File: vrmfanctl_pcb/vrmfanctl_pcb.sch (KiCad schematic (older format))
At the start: 7 parts, among them J1 SATA Power Male, J2 Hole, J3 Pin socket L-shape, J4 Pin socket L-shape, U1 ATtiny85-20PU

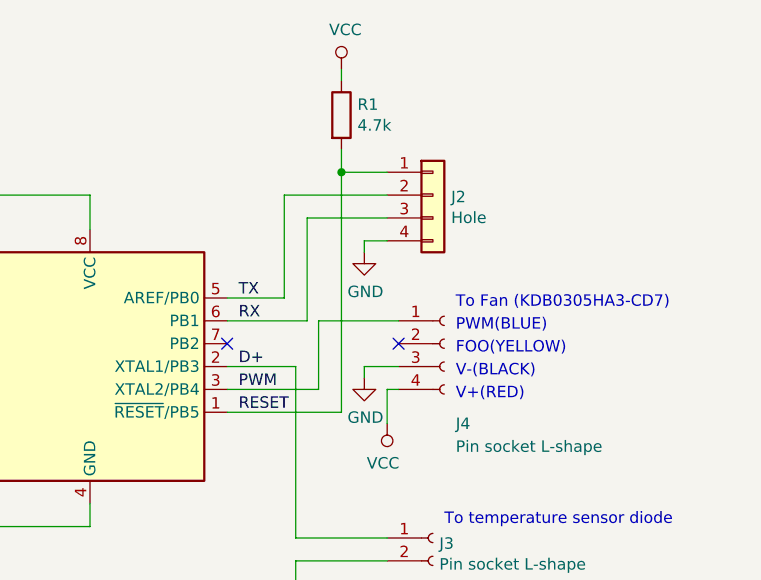
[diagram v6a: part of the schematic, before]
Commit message: rewrite firmware and update pcb
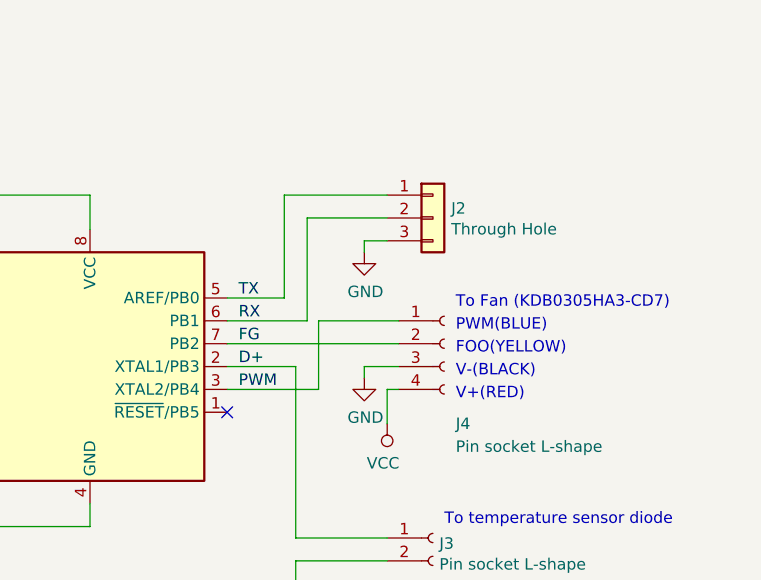
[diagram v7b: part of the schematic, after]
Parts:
- removed J2: Hole, Connector_PinHeader_2.54mm:PinHeader_1x04_P2.54mm_Vertical, symbol Connector_Generic:Conn_01x04
- removed R1: 4.7k, Resistor_THT:R_Axial_DIN0204_L3.6mm_D1.6mm_P5.08mm_Horizontal, symbol Device:R
- added J2: Through Hole, Connector_PinHeader_2.54mm:PinHeader_1x03_P2.54mm_Vertical, symbol Connector_Generic:Conn_01x03
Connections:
- net GND: now also J2.3 (Pin_3)
- net RX: now also J2.2 (Pin_2)
- net TX: now also J2.1 (Pin_1)
- net FG: now reaches U1.7 (PB2)
- net FG: now also J4.2 (Pin_2)
- net RESET: no longer names the net of U1.1 (~RESET~/PB5)
- no-connect marks 11 -> 10
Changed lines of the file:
@@
 EESchema Schematic File Version 4
 LIBS:vrmfanctl_pcb-cache
-EELAYER 26 0
+EELAYER 30 0
 EELAYER END
 $Descr A4 11693 8268
@@
 $EndComp
 $Comp
+L power:GND #PWR06
+U 1 1 5D600CEB
+P 5700 1600
+F 0 "#PWR06" H 5700 1350 50  0001 C CNN
+F 1 "GND" H 5705 1427 50  0000 C CNN
+F 2 "" H 5700 1600 50  0001 C CNN
+F 3 "" H 5700 1600 50  0001 C CNN
+	1    5700 1600
+	1    0    0    -1
+$EndComp
+Wire Wire Line
+	5800 1550 5700 1550
+Wire Wire Line
+	5700 1550 5700 1600
+Wire Wire Line
+	5350 1350 5350 1800
+Wire Wire Line
+	5350 1800 5100 1800
+Wire Wire Line
+	5350 1350 5800 1350
+Text Label 5150 1800 0    50   ~ 0
+TX
+Text Label 5150 1900 0    50   ~ 0
+RX
+Wire Wire Line
+	5100 1900 5450 1900
+Wire Wire Line
+	5450 1900 5450 1450
+Wire Wire Line
+	5450 1450 5800 1450
+Wire Wire Line
+	5850 1900 5500 1900
+Text Notes 6050 2800 0    50   ~ 0
+To temperature sensor diode
+Text Label 5150 2100 0    50   ~ 0
+D+
+Wire Wire Line
+	5400 2850 5800 2850
+Wire Wire Line
+	5400 2950 5400 3050
+Wire Wire Line
+	5800 2950 5400 2950
+$Comp
+L power:GND #PWR05
+U 1 1 5D614B08
+P 5400 3050
+F 0 "#PWR05" H 5400 2800 50  0001 C CNN
+F 1 "GND" H 5405 2877 50  0000 C CNN
+F 2 "" H 5400 3050 50  0001 C CNN
+F 3 "" H 5400 3050 50  0001 C CNN
+	1    5400 3050
+	1    0    0    -1
+$EndComp
+$Comp
+L Connector:Conn_01x02_Female J3
+U 1 1 5D610DF4
+P 6000 2850
+F 0 "J3" H 6028 2826 50  0000 L CNN
+F 1 "Pin socket L-shape" H 6028 2735 50  0000 L CNN
+F 2 "Connector_PinSocket_2.54mm:PinSocket_1x02_P2.54mm_Horizontal" H 6000 2850 50  0001 C CNN
+F 3 "~" H 6000 2850 50  0001 C CNN
+	1    6000 2850
+	1    0    0    -1
+$EndComp
+Wire Wire Line
+	5500 2200 5400 2200
+Wire Wire Line
+	5400 2200 5100 2200
+Wire Wire Line
+	5400 2100 5100 2100
+Wire Wire Line
+	5400 2100 5400 2850
+Wire Wire Line
+	5500 1900 5500 2200
+$Comp
 L Connector:Conn_01x04_Female J4
 U 1 1 5D5F6860
@@
 	1    0    0    -1
 $EndComp
-$Comp
-L power:GND #PWR06
-U 1 1 5D600CEB
-P 5700 1600
-F 0 "#PWR06" H 5700 1350 50  0001 C CNN
-F 1 "GND" H 5705 1427 50  0000 C CNN
-F 2 "" H 5700 1600 50  0001 C CNN
-F 3 "" H 5700 1600 50  0001 C CNN
-	1    5700 1600
-	1    0    0    -1
-$EndComp
-Wire Wire Line
-	5800 1550 5700 1550
-Wire Wire Line
-	5700 1550 5700 1600
-Wire Wire Line
-	5350 1350 5350 1800
-Wire Wire Line
-	5350 1800 5100 1800
-Wire Wire Line
-	5350 1350 5800 1350
-Text Label 5150 1800 0    50   ~ 0
-TX
-Text Label 5150 1900 0    50   ~ 0
-RX
-Wire Wire Line
-	5100 1900 5450 1900
-Wire Wire Line
-	5450 1900 5450 1450
-Wire Wire Line
-	5450 1450 5800 1450
-Wire Wire Line
-	5850 1900 5500 1900
-Text Notes 6050 2800 0    50   ~ 0
-To temperature sensor diode
-Text Label 5150 2100 0    50   ~ 0
-D+
-Wire Wire Line
-	5400 2850 5800 2850
-Wire Wire Line
-	5400 2950 5400 3050
-Wire Wire Line
-	5800 2950 5400 2950
-$Comp
-L power:GND #PWR05
-U 1 1 5D614B08
-P 5400 3050
-F 0 "#PWR05" H 5400 2800 50  0001 C CNN
-F 1 "GND" H 5405 2877 50  0000 C CNN
-F 2 "" H 5400 3050 50  0001 C CNN
-F 3 "" H 5400 3050 50  0001 C CNN
-	1    5400 3050
-	1    0    0    -1
-$EndComp
-$Comp
-L Connector:Conn_01x02_Female J3
-U 1 1 5D610DF4
-P 6000 2850
-F 0 "J3" H 6028 2826 50  0000 L CNN
-F 1 "Pin socket L-shape" H 6028 2735 50  0000 L CNN
-F 2 "Connector_PinSocket_2.54mm:PinSocket_1x02_P2.54mm_Horizontal" H 6000 2850 50  0001 C CNN
-F 3 "~" H 6000 2850 50  0001 C CNN
-	1    6000 2850
-	1    0    0    -1
-$EndComp
-Wire Wire Line
-	5500 2200 5400 2200
-Wire Wire Line
-	5400 2200 5100 2200
-Wire Wire Line
-	5400 2100 5100 2100
-Wire Wire Line
-	5400 2100 5400 2850
-NoConn ~ 5100 2000
-NoConn ~ 5850 2000
-$Comp
-L Device:R R1
-U 1 1 5D62348B
-P 5600 1000
-F 0 "R1" H 5670 1046 50  0000 L CNN
-F 1 "4.7k" H 5670 955 50  0000 L CNN
-F 2 "Resistor_THT:R_Axial_DIN0204_L3.6mm_D1.6mm_P5.08mm_Horizontal" V 5530 1000 50  0001 C CNN
-F 3 "~" H 5600 1000 50  0001 C CNN
-	1    5600 1000
-	1    0    0    -1
-$EndComp
-$Comp
-L Connector_Generic:Conn_01x04 J2
-U 1 1 5D6235F9
-P 6000 1350
-F 0 "J2" H 6080 1342 50  0000 L CNN
-F 1 "Hole" H 6080 1251 50  0000 L CNN
-F 2 "Connector_PinHeader_2.54mm:PinHeader_1x04_P2.54mm_Vertical" H 6000 1350 50  0001 C CNN
-F 3 "~" H 6000 1350 50  0001 C CNN
-	1    6000 1350
-	1    0    0    -1
-$EndComp
-$Comp
-L power:VCC #PWR0103
-U 1 1 5D623D93
-P 5600 800
-F 0 "#PWR0103" H 5600 650 50  0001 C CNN
-F 1 "VCC" H 5617 973 50  0000 C CNN
-F 2 "" H 5600 800 50  0001 C CNN
-F 3 "" H 5600 800 50  0001 C CNN
-	1    5600 800
-	1    0    0    -1
-$EndComp
-Wire Wire Line
-	5600 800  5600 850
-Wire Wire Line
-	5600 1150 5600 1250
-Wire Wire Line
-	5600 1250 5800 1250
-Wire Wire Line
-	5500 1900 5500 2200
-Wire Wire Line
-	5600 1250 5600 2300
-Wire Wire Line
-	5600 2300 5100 2300
-Connection ~ 5600 1250
-Text Label 5150 2300 0    50   ~ 0
-RESET
+Wire Wire Line
+	5100 2000 5850 2000
+Text Label 5150 2000 0    50   ~ 0
+FG
+$Comp
+L Connector_Generic:Conn_01x03 J2
+U 1 1 5D6F20BE
+P 6000 1450
+F 0 "J2" H 6080 1492 50  0000 L CNN
+F 1 "Through Hole" H 6080 1401 50  0000 L CNN
+F 2 "Connector_PinHeader_2.54mm:PinHeader_1x03_P2.54mm_Vertical" H 6000 1450 50  0001 C CNN
+F 3 "~" H 6000 1450 50  0001 C CNN
+	1    6000 1450
+	1    0    0    -1
+$EndComp
+NoConn ~ 5100 2300
 $EndSCHEMATC

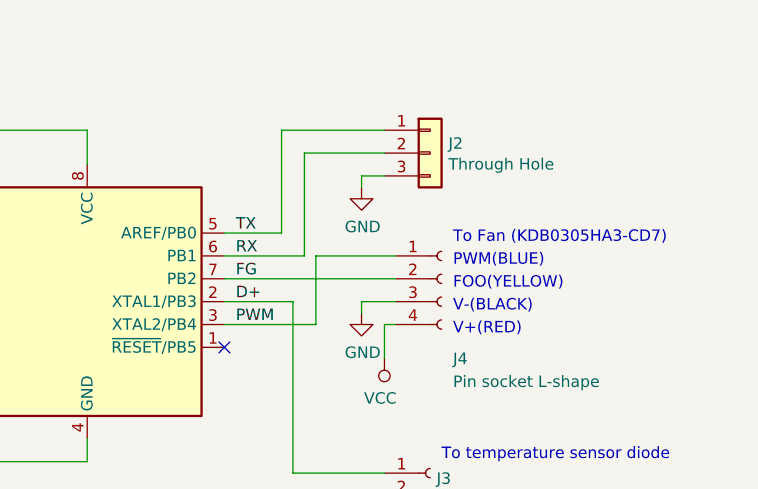
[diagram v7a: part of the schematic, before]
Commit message: change pcb layout
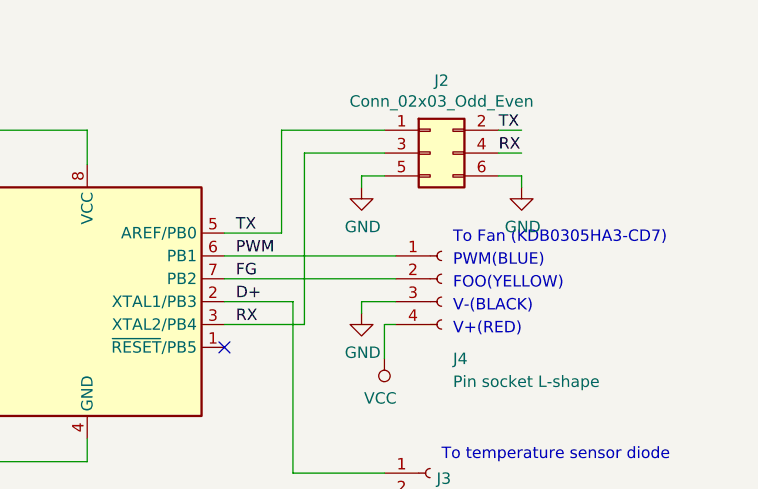
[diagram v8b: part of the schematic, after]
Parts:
- removed J2: Through Hole, Connector_PinHeader_2.54mm:PinHeader_1x03_P2.54mm_Vertical, symbol Connector_Generic:Conn_01x03
- added J2: Conn_02x03_Odd_Even, symbol Connector_Generic:Conn_02x03_Odd_Even
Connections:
- wire segments 46 -> 47
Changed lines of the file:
@@
 Text Notes 6100 1850 0    50   ~ 0
 To Fan (KDB0305HA3-CD7)
-Text Label 5150 2200 0    50   ~ 0
-PWM
 Wire Wire Line
 	5700 2100 5850 2100
@@
 Text Label 5150 1800 0    50   ~ 0
 TX
-Text Label 5150 1900 0    50   ~ 0
+Text Label 5150 2200 0    50   ~ 0
 RX
-Wire Wire Line
-	5100 1900 5450 1900
-Wire Wire Line
-	5450 1900 5450 1450
-Wire Wire Line
-	5450 1450 5800 1450
-Wire Wire Line
-	5850 1900 5500 1900
 Text Notes 6050 2800 0    50   ~ 0
 To temperature sensor diode
@@
 $EndComp
 Wire Wire Line
-	5500 2200 5400 2200
-Wire Wire Line
-	5400 2200 5100 2200
-Wire Wire Line
 	5400 2100 5100 2100
 Wire Wire Line
 	5400 2100 5400 2850
-Wire Wire Line
-	5500 1900 5500 2200
 $Comp
 L Connector:Conn_01x04_Female J4
@@
 	1    0    0    -1
 $EndComp
+Wire Wire Line
+	5100 2000 5850 2000
+Text Label 5150 2000 0    50   ~ 0
+FG
+NoConn ~ 5100 2300
+Text Label 5150 1900 0    50   ~ 0
+PWM
+Wire Wire Line
+	5100 1900 5850 1900
 $Comp
 L MCU_Microchip_ATtiny:ATtiny85-20PU U1
@@
 $EndComp
 Wire Wire Line
-	5100 2000 5850 2000
-Text Label 5150 2000 0    50   ~ 0
-FG
-$Comp
-L Connector_Generic:Conn_01x03 J2
-U 1 1 5D6F20BE
+	5100 2200 5450 2200
+Wire Wire Line
+	5450 2200 5450 1450
+Wire Wire Line
+	5450 1450 5800 1450
+$Comp
+L power:GND #PWR0103
+U 1 1 5D8DD390
+P 6400 1600
+F 0 "#PWR0103" H 6400 1350 50  0001 C CNN
+F 1 "GND" H 6405 1427 50  0000 C CNN
+F 2 "" H 6400 1600 50  0001 C CNN
+F 3 "" H 6400 1600 50  0001 C CNN
+	1    6400 1600
+	1    0    0    -1
+$EndComp
+Wire Wire Line
+	6400 1600 6400 1550
+Wire Wire Line
+	6400 1550 6300 1550
+Wire Wire Line
+	6300 1450 6400 1450
+Wire Wire Line
+	6300 1350 6400 1350
+Text Label 6300 1350 0    50   ~ 0
+TX
+Text Label 6300 1450 0    50   ~ 0
+RX
+$Comp
+L Connector_Generic:Conn_02x03_Odd_Even J2
+U 1 1 5D8E20EB
 P 6000 1450
-F 0 "J2" H 6080 1492 50  0000 L CNN
-F 1 "Through Hole" H 6080 1401 50  0000 L CNN
-F 2 "Connector_PinHeader_2.54mm:PinHeader_1x03_P2.54mm_Vertical" H 6000 1450 50  0001 C CNN
+F 0 "J2" H 6050 1767 50  0000 C CNN
+F 1 "Conn_02x03_Odd_Even" H 6050 1676 50  0000 C CNN
+F 2 "" H 6000 1450 50  0001 C CNN
 F 3 "~" H 6000 1450 50  0001 C CNN
 	1    6000 1450
 	1    0    0    -1
 $EndComp
-NoConn ~ 5100 2300
 $EndSCHEMATC
